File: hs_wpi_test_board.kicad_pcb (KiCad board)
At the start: 2 copper layers, 33 parts, among them Q1 Q_NPN_EBC, Q10 Q_NPN_EBC, Q2 Q_NPN_EBC, Q3 Q_NPN_EBC, Q4 Q_NPN_EBC, Q5 Q_NPN_EBC, Q6 Q_NPN_EBC, Q7 Q_NPN_EBC, Q8 Q_NPN_EBC, Q9 Q_NPN_EBC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

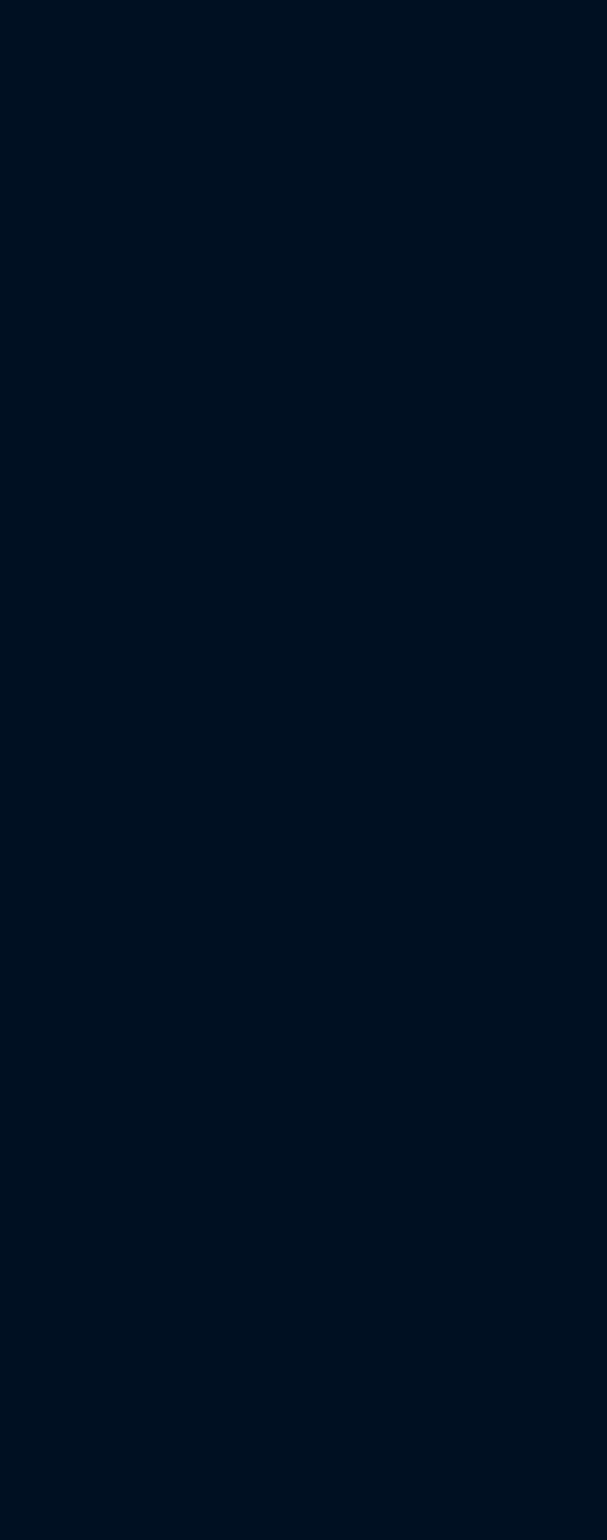
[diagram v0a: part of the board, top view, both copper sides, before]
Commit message: angled socket
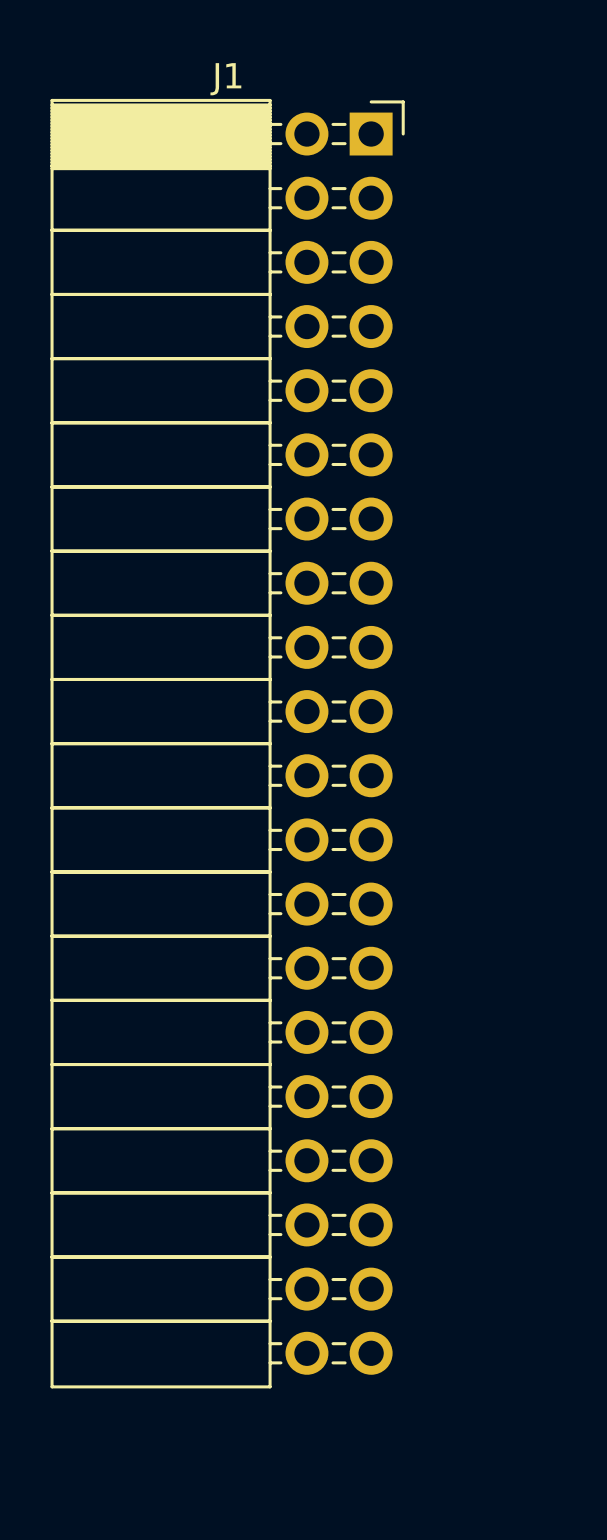
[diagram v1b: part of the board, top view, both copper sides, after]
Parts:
- added J1: Raspberry_Pi_2_3, Socket_Strips:Socket_Strip_Angled_2x20_Pitch2.54mm, F.Cu at (0.00, 0.00)

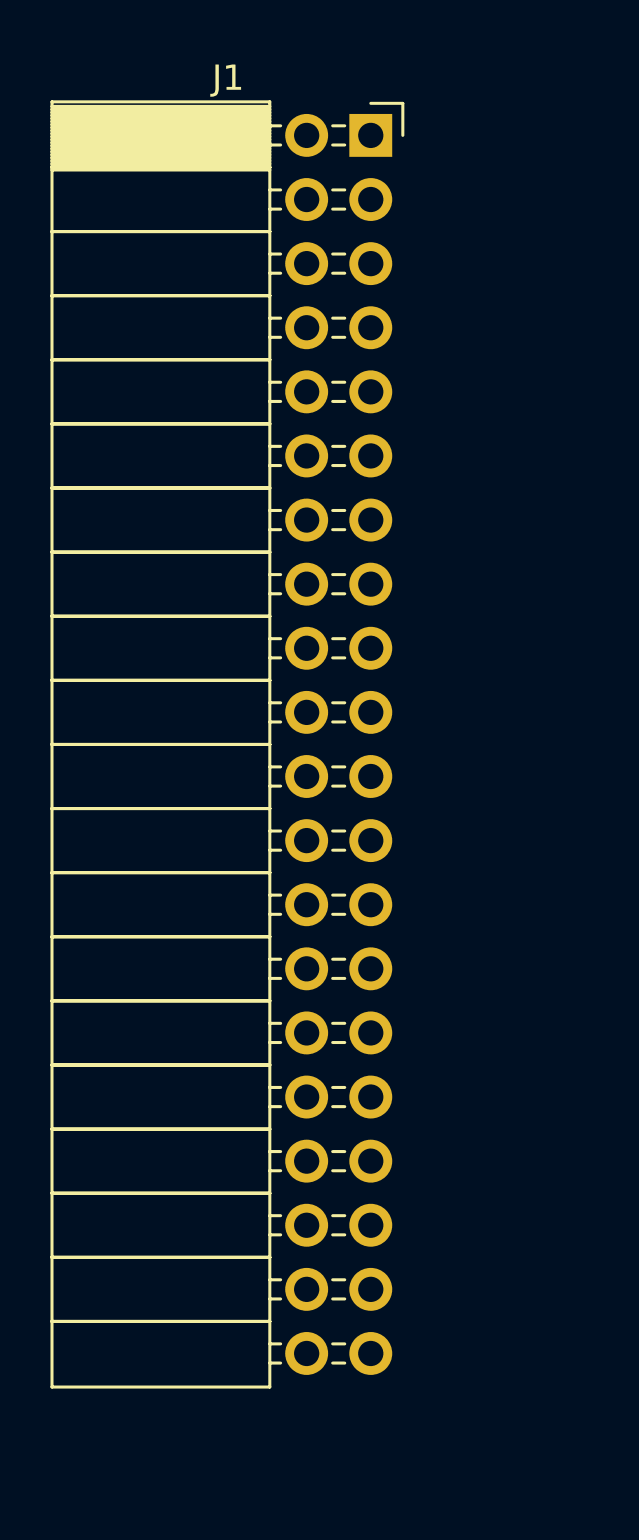
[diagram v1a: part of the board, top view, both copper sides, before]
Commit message: pin header straight
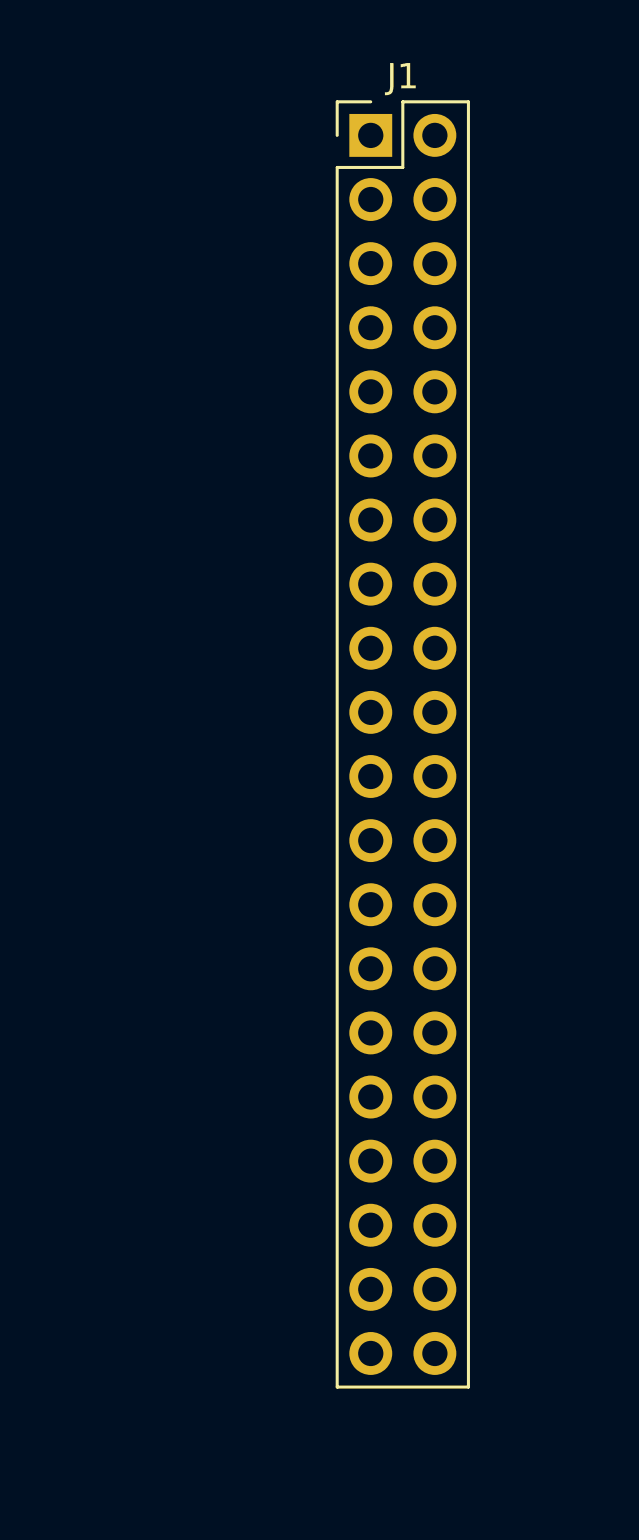
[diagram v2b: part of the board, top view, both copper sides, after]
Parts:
- J1: footprint Socket_Strips:Socket_Strip_Angled_2x20_Pitch2.54mm -> Pin_Headers:Pin_Header_Straight_2x20_Pitch2.54mm

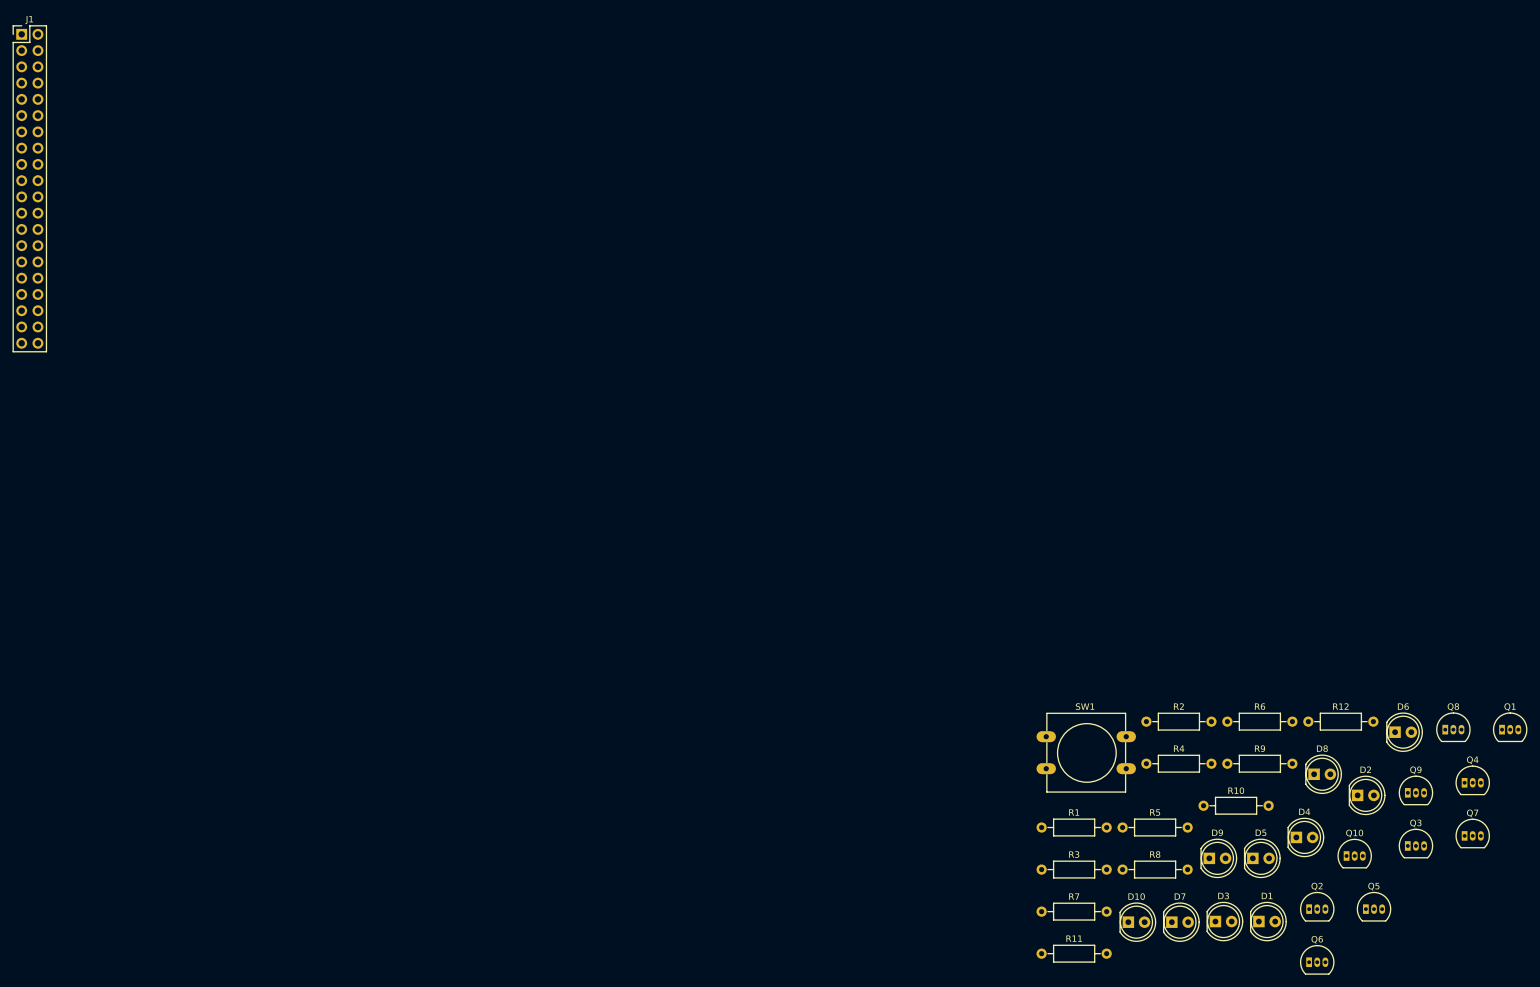
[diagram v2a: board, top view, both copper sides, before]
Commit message: place components
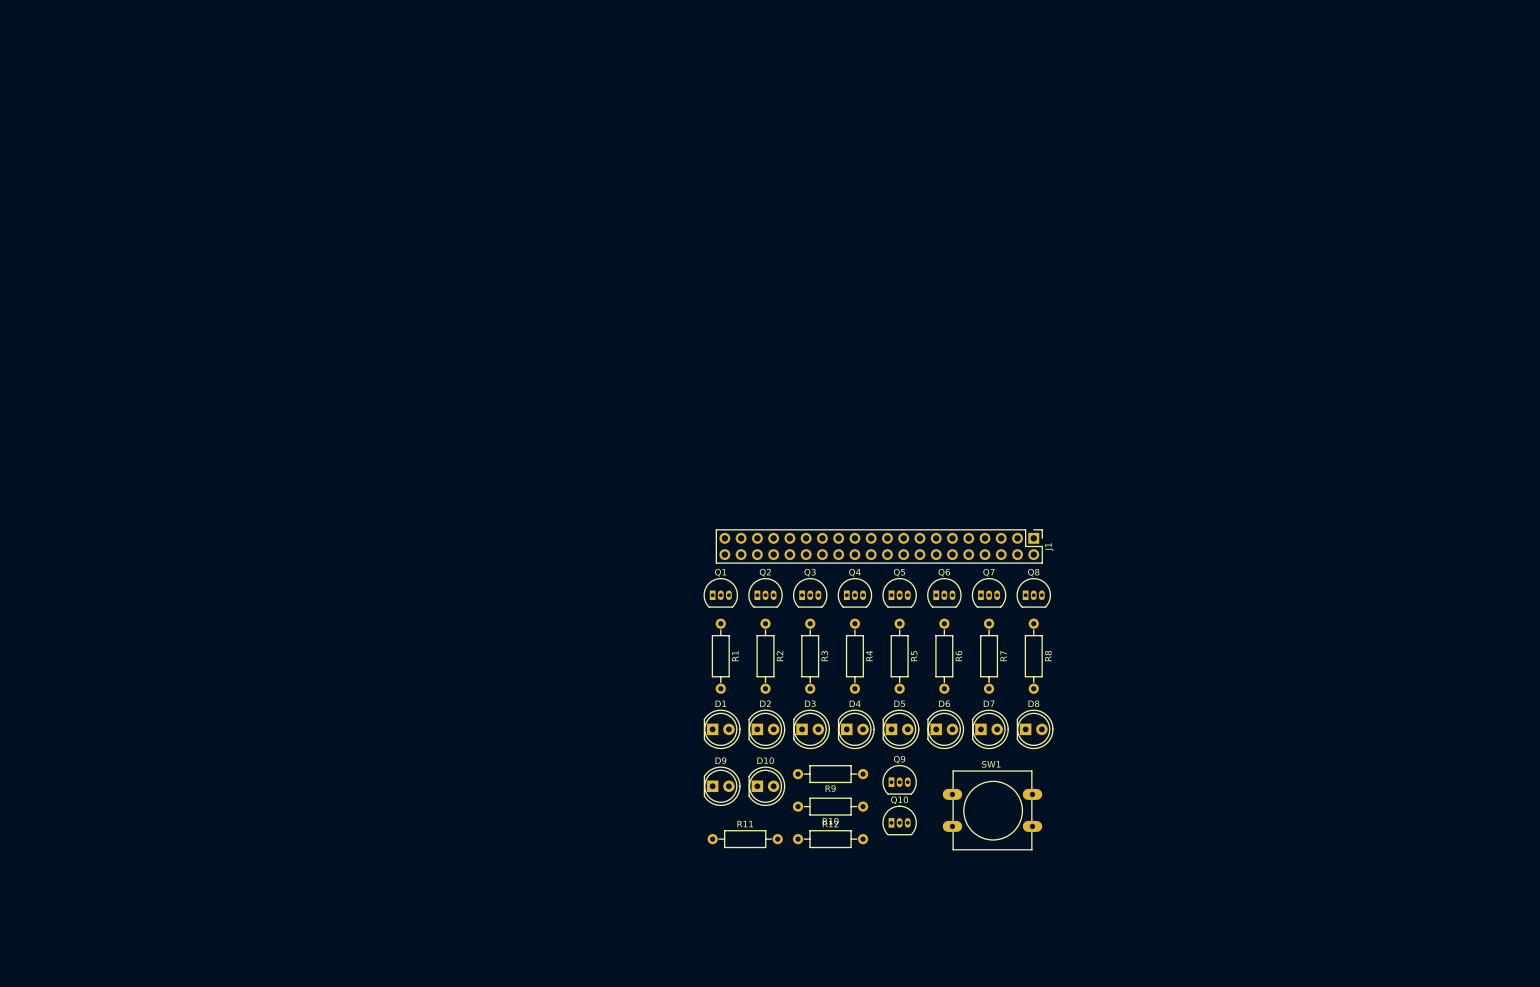
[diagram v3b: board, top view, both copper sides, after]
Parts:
- moved J1 176.6 mm to (158.1, 78.7), turned to 270 degrees
- moved Q1 125.1 mm to (108.0, 87.6)
- moved Q3 102.4 mm to (121.9, 87.6)
- moved Q4 100.9 mm to (128.9, 87.6)
- moved Q2 99.2 mm to (114.9, 87.6)
- moved D2 94.3 mm to (114.9, 108.6)
- moved D1 90.5 mm to (108.0, 108.6)
- moved Q5 88.9 mm to (135.9, 87.6)
- moved Q7 84.4 mm to (149.9, 87.6)
- moved R12 81.8 mm to (121.3, 125.7)
- moved Q6 81.7 mm to (142.9, 87.6)
- moved Q9 80.7 mm to (135.9, 116.8)
- moved D9 78.4 mm to (108.0, 117.5)
- moved D4 72.2 mm to (128.9, 108.6)
- moved D6 71.7 mm to (142.9, 108.6)
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
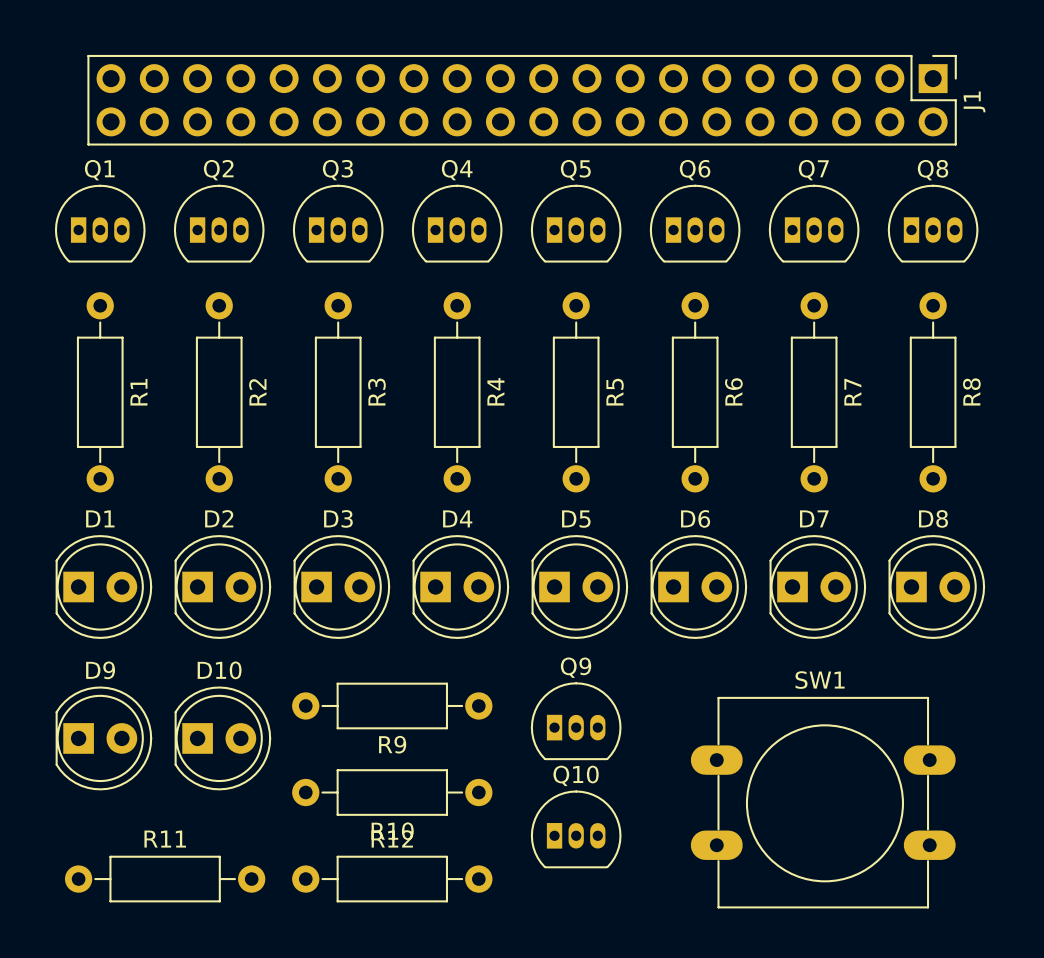
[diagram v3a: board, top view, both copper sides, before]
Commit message: add board outline
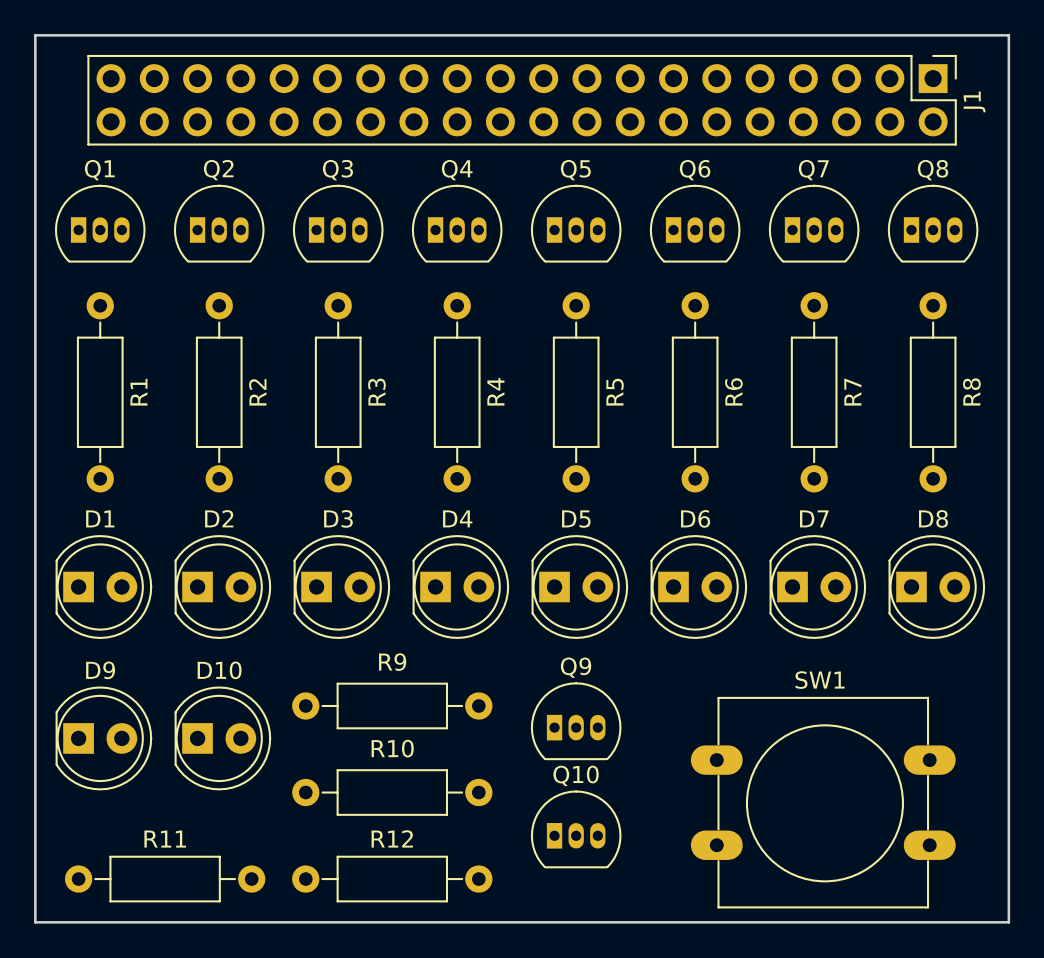
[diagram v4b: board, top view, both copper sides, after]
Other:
- board outline added: 57.2 x 52.1 mm
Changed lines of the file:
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@@
     (area 0 0 0 0)
     (thickness 1.6)
-    (drawings 0)
+    (drawings 4)
     (tracks 0)
     (zones 0)
@@
     (descr "Resistor, Axial_DIN0207 series, Axial, Horizontal, pin pitch=10.16mm, 0.25W = 1/4W, length*diameter=6.3*2.5mm^2, http://cdn-reichelt.de/documents/datenblatt/B400/1_4W%23YAG.pdf")
     (tags "Resistor Axial_DIN0207 series Axial Horizontal pin pitch 10.16mm 0.25W = 1/4W length 6.3mm diameter 2.5mm")
-    (fp_text reference R9 (at 5.08 -2.31 180) (layer F.SilkS)
+    (fp_text reference R9 (at 5.08 2.54 180) (layer F.SilkS)
       (effects (font (size 1 1) (thickness 0.15)))
     )
@@
     (descr "Resistor, Axial_DIN0207 series, Axial, Horizontal, pin pitch=10.16mm, 0.25W = 1/4W, length*diameter=6.3*2.5mm^2, http://cdn-reichelt.de/documents/datenblatt/B400/1_4W%23YAG.pdf")
     (tags "Resistor Axial_DIN0207 series Axial Horizontal pin pitch 10.16mm 0.25W = 1/4W length 6.3mm diameter 2.5mm")
-    (fp_text reference R10 (at 5.08 -2.31 180) (layer F.SilkS)
+    (fp_text reference R10 (at 5.08 2.54 180) (layer F.SilkS)
       (effects (font (size 1 1) (thickness 0.15)))
     )
@@
     )
   )
+  (gr_line (start 105.41 128.27) (end 105.41 76.2) (angle 90) (layer Edge.Cuts) (width 0.15))
+  (gr_line (start 162.56 128.27) (end 105.41 128.27) (angle 90) (layer Edge.Cuts) (width 0.15))
+  (gr_line (start 162.56 76.2) (end 162.56 128.27) (angle 90) (layer Edge.Cuts) (width 0.15))
+  (gr_line (start 105.41 76.2) (end 162.56 76.2) (angle 90) (layer Edge.Cuts) (width 0.15))
 )

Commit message: routed some stuff
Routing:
- net VCC: track 0.00 -> 144.4 mm
- net Net-(J1-Pad31): track 0.00 -> 88.7 mm, vias 0 -> 1
- net /Button: track 0.00 -> 64.1 mm, vias 0 -> 1
- net Net-(J1-Pad29): track 0.00 -> 61.8 mm
- net /PWM1: track 0.00 -> 54.2 mm
- net /PWM0: track 0.00 -> 42.8 mm, vias 0 -> 1
- net /WPi0: track 0.00 -> 40.5 mm
- net /WPi6: track 0.00 -> 35.6 mm, vias 0 -> 1
- net /WPi1: track 0.00 -> 32.0 mm
- net Net-(R12-Pad2): track 0.00 -> 30.0 mm
- net /WPi2: track 0.00 -> 25.4 mm, vias 0 -> 1
- net /WPi5: track 0.00 -> 22.1 mm, vias 0 -> 1
- net /WPi3: track 0.00 -> 15.0 mm, vias 0 -> 1
- net /WPi7: track 0.00 -> 13.0 mm
- net Net-(D9-Pad2): track 0.00 -> 11.6 mm
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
